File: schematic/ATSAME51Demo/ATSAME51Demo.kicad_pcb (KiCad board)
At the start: 4 copper layers, 100 x 100 mm, 69 parts, among them IC1 ATSAME51J20A-AU, IC2 AZ1117IH-3.3TRG1, IC3 MCP2221-I_SL, J1 Barrel_Jack_Switch, J10 Conn_02x06_Odd_Even, J11 Conn_02x07_Odd_Even, J12 Conn_01x02, J13 Conn_01x08, J14 Conn_02x08_Odd_Even, J15 Conn_02x06_Odd_Even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

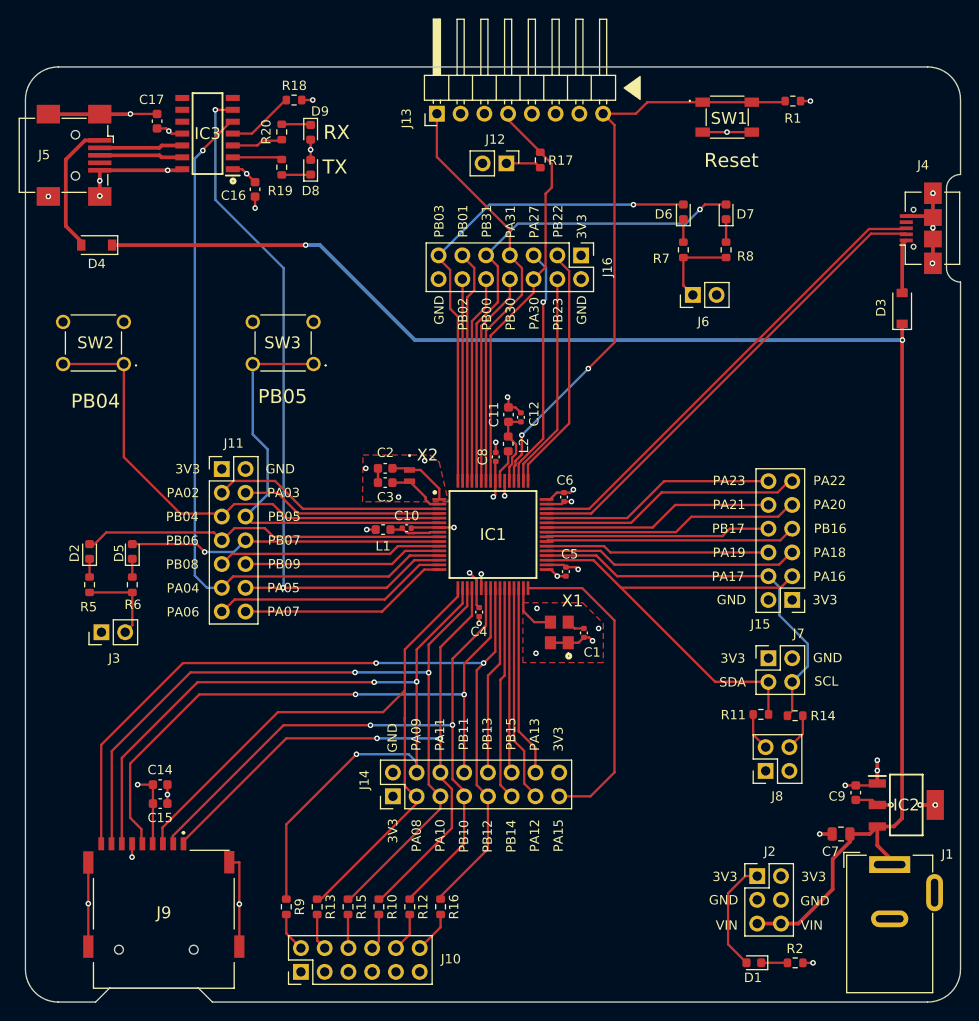
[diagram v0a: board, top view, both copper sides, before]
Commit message: Added  USB_VBUS_SENSE
And other minor improvements
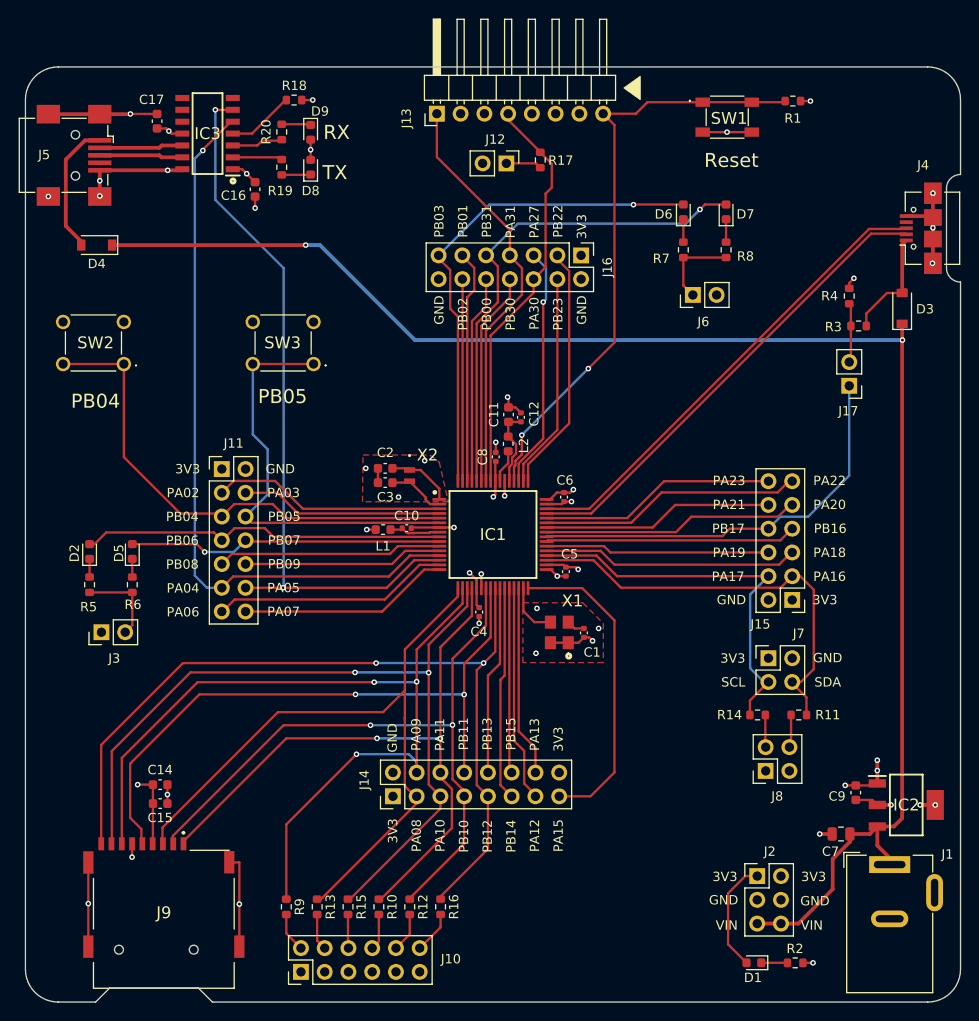
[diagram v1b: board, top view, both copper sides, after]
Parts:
- added J17: Conn_01x02, Connector_PinHeader_2.54mm:PinHeader_1x02_P2.54mm_Vertical, F.Cu at (138.1, 94.1)
- added R3: 15k, Resistor_SMD:R_0603_1608Metric, F.Cu at (139.1, 87.7)
- added R4: 22k, Resistor_SMD:R_0603_1608Metric, F.Cu at (138.1, 84.5)
- R7: value 220R -> 62R
- moved R11 4.05 mm to (132.7, 129.3)
- moved R14 4.01 mm to (128.3, 129.3)
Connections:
- J7 pad 3: SERCOM1_PAD0 -> SERCOM1_PAD1
- J7 pad 4: SERCOM1_PAD1 -> SERCOM1_PAD0
- R11 pad 2: Net-(J8-Pad2) -> Net-(J8-Pad4)
- R14 pad 2: Net-(J8-Pad4) -> Net-(J8-Pad2)
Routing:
- net PB17: track 24.1 -> 44.7 mm
- net Net-(J17-Pad2): track 0.00 -> 6.38 mm
- net Net-(D3-Pad2): track 6.28 -> 12.4 mm
- net SERCOM1_PAD0: track 51.4 -> 46.6 mm
- net GND: track 92.0 -> 93.3 mm, vias 33 -> 34
- net Net-(J8-Pad2): track 4.05 -> 3.46 mm
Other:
- board text added: "Jumpers J3, J6 = LED enable J8 = I2C pull-ups J10 = SD card pull-ups J12 = SWCLK pull-up J17 = USB_VBUS_SENSE enable"
- board text removed: "Jumpers J3, J6 = LED enable J8 = I2C pull-ups J10 = SD card pull-ups J12 = SWCLK pull-up"

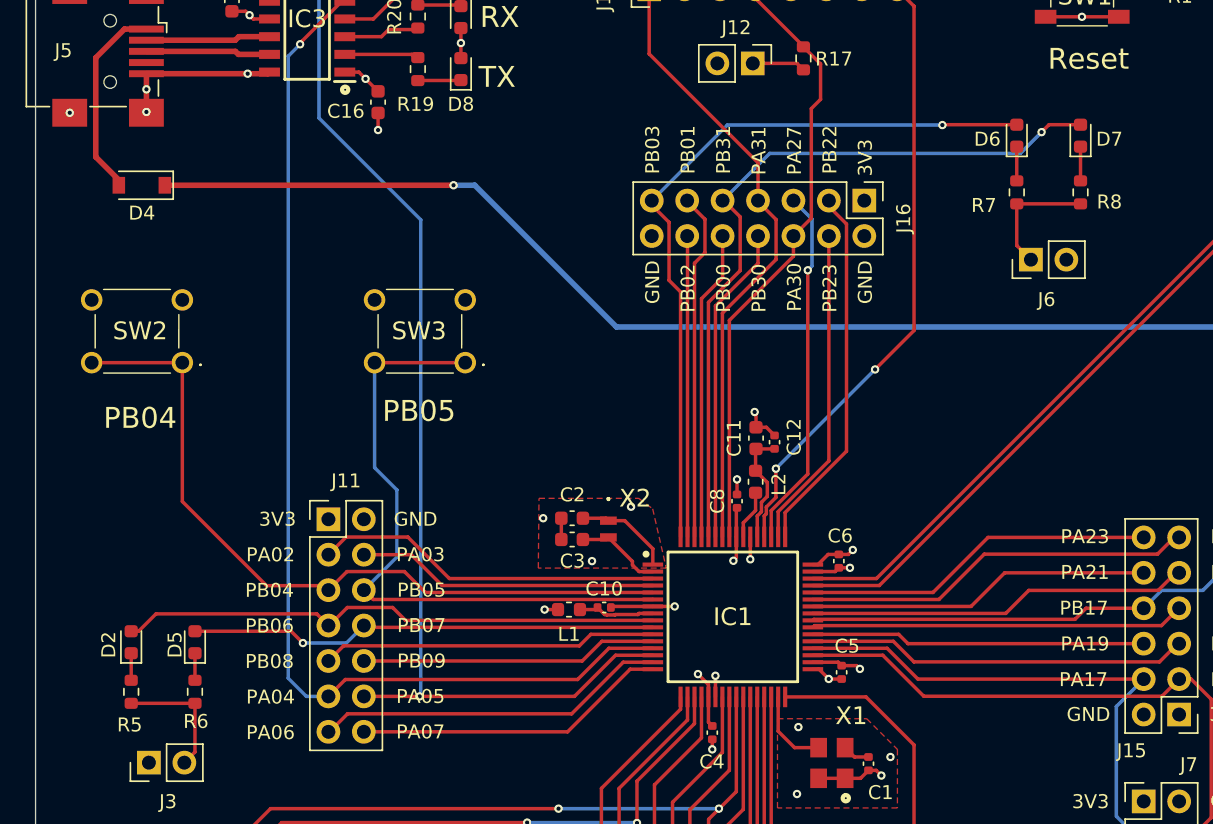
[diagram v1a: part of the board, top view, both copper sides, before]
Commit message: Changed leds to 0805
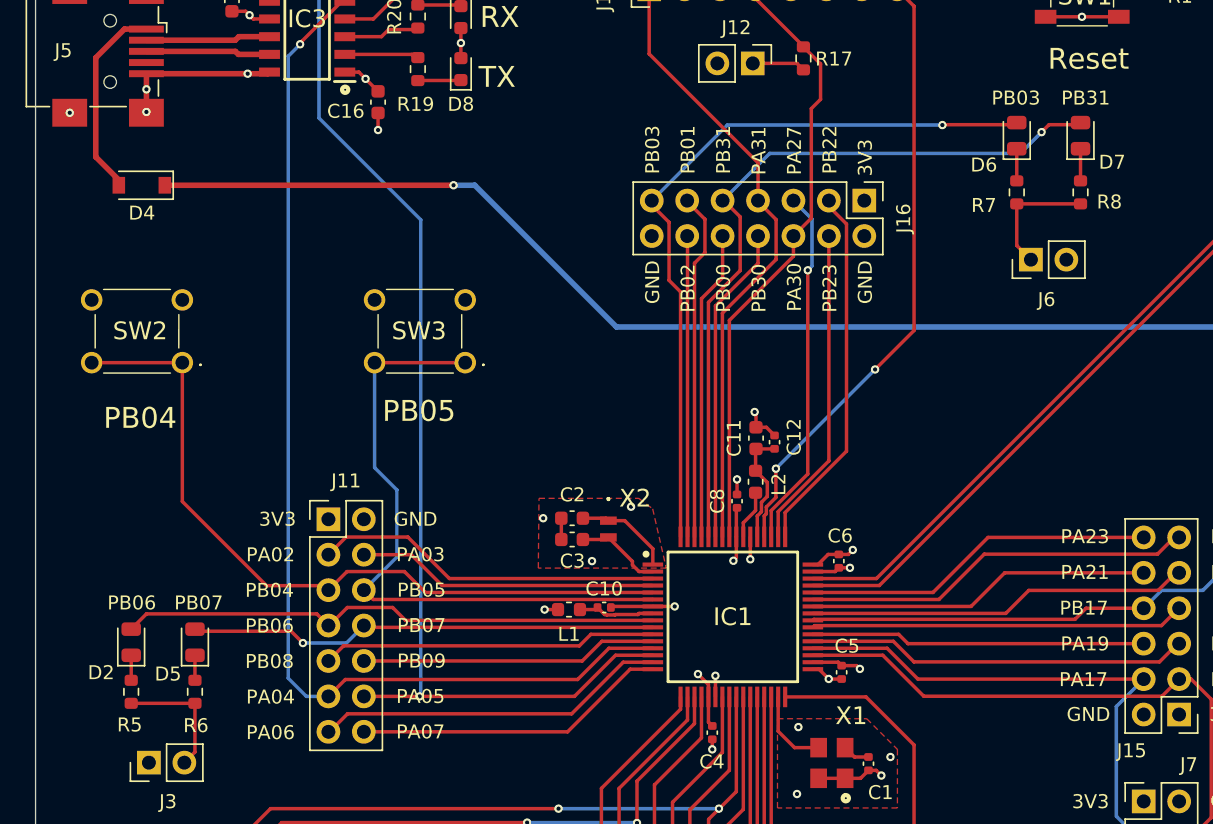
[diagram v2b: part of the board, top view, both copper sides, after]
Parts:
- D2, D5, D6, D7: footprint LED_SMD:LED_0603_1608Metric -> LED_SMD:LED_0805_2012Metric

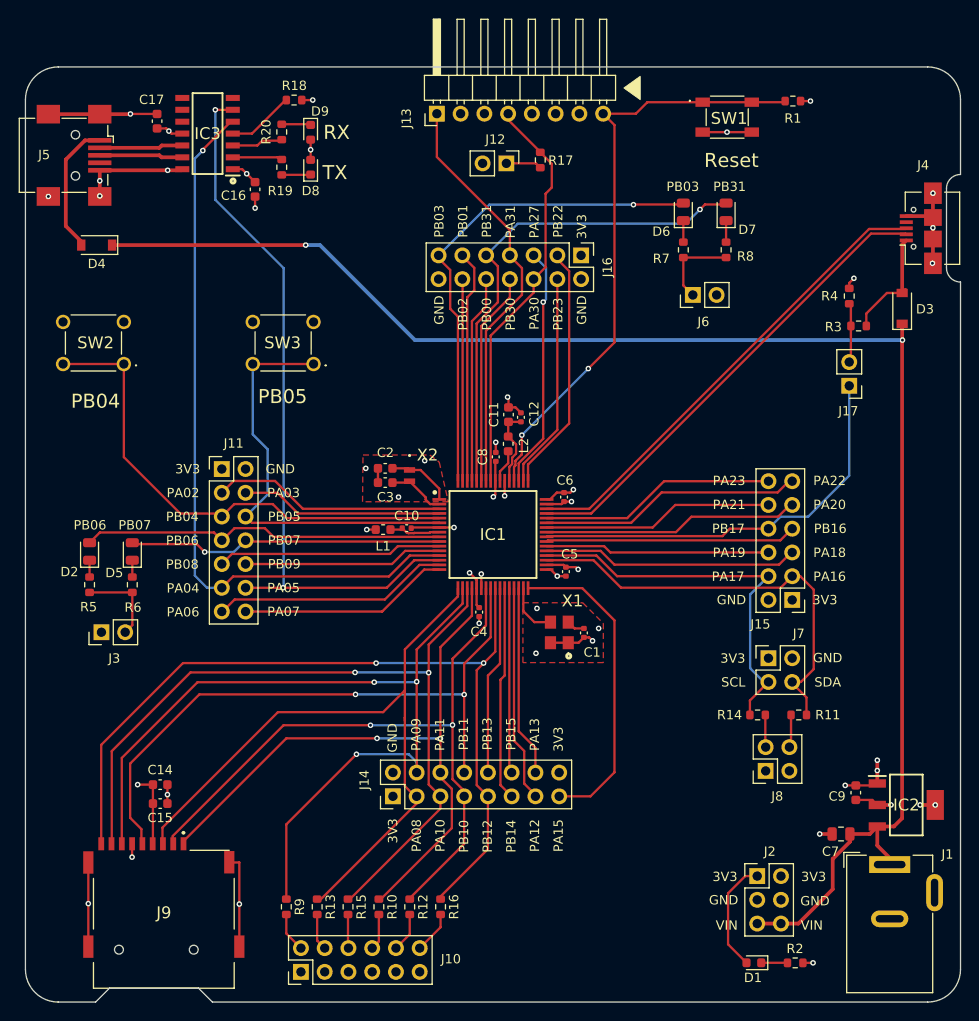
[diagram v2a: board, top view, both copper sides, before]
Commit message: Converted to KiCad 6
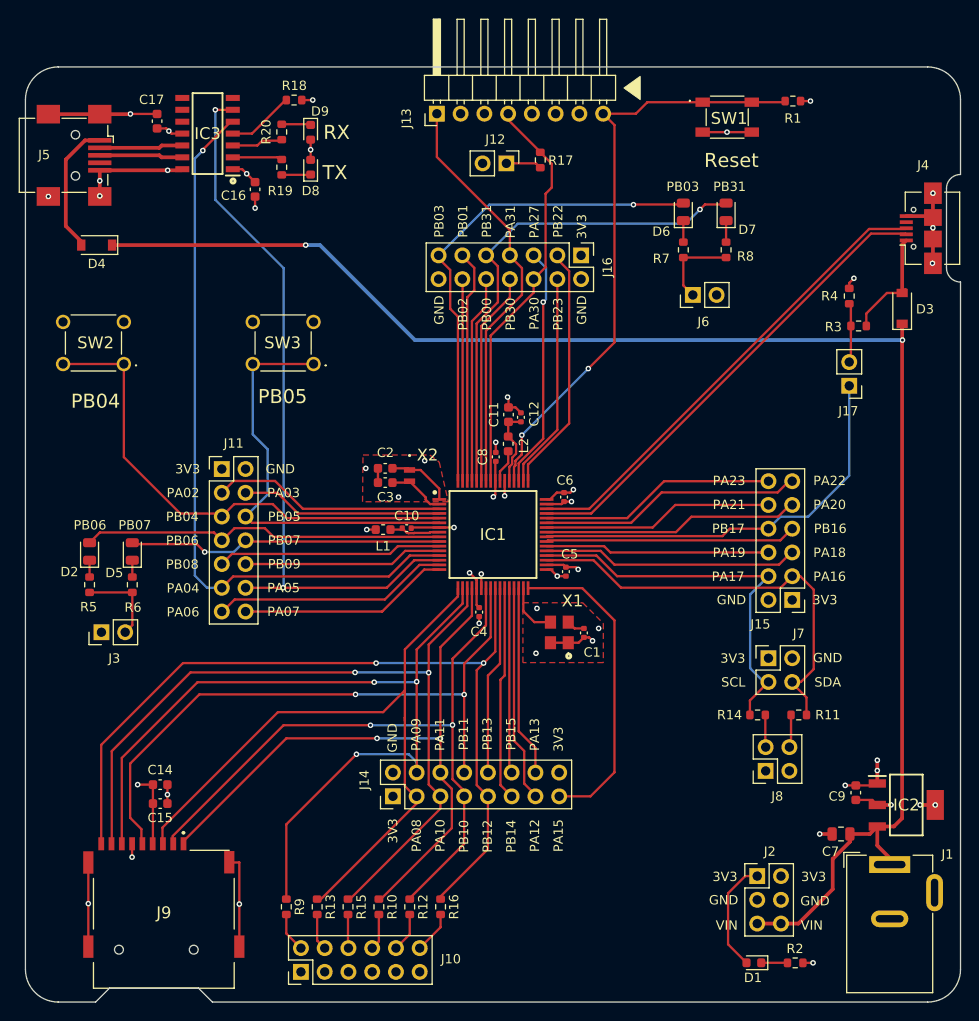
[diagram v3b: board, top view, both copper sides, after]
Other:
- net class Default removed
- net class Power removed
